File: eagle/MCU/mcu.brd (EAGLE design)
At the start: 100 x 60 mm, 87 parts, among them IC1 HCT4046A, IC10 LD117ADT50TR, IC2 AZ1117-3.3, IC3 4059D, IC4 AZ1086, IC5 74AHCT1G08DCK, IC7 74LVX4245TSSOP24W, IC8 74LVX4245TSSOP24W, IC9 74LVX4245TSSOP24W, T1 2N7002E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

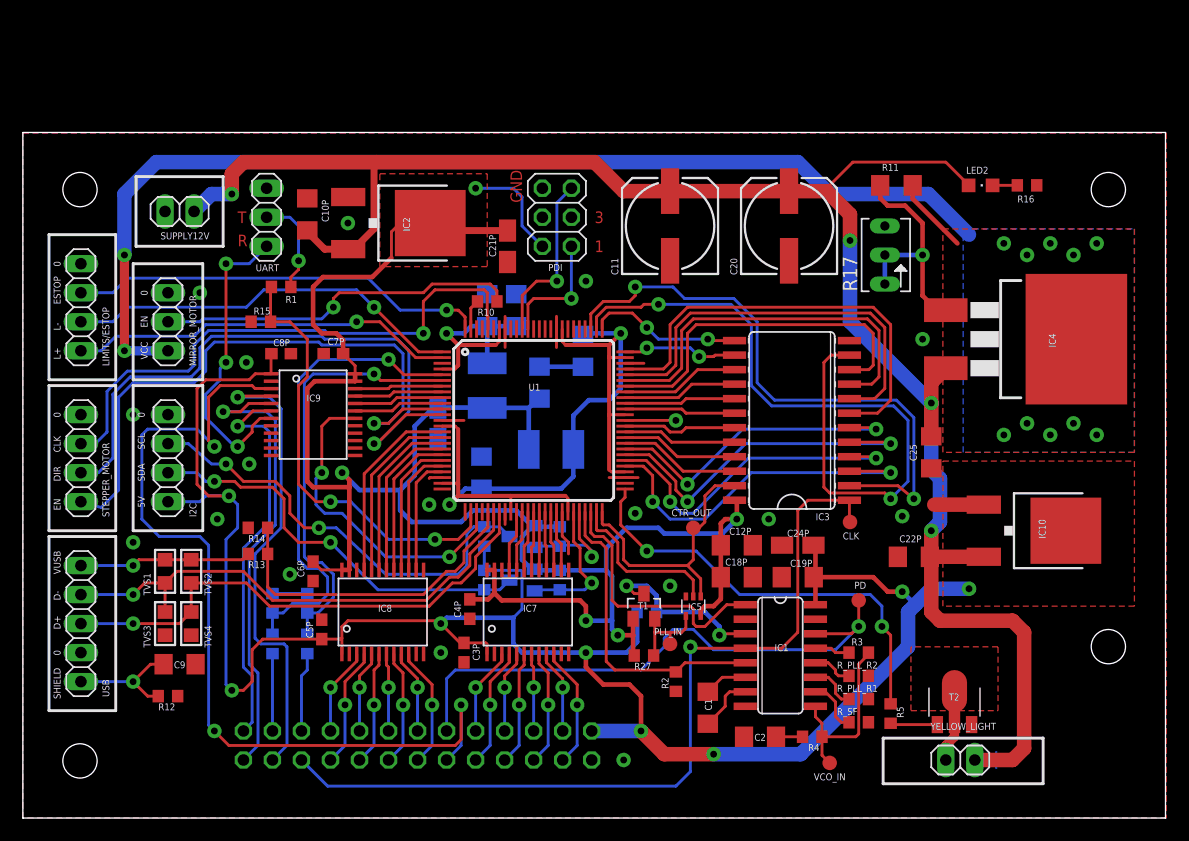
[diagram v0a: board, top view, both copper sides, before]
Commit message: PLL acquires lock
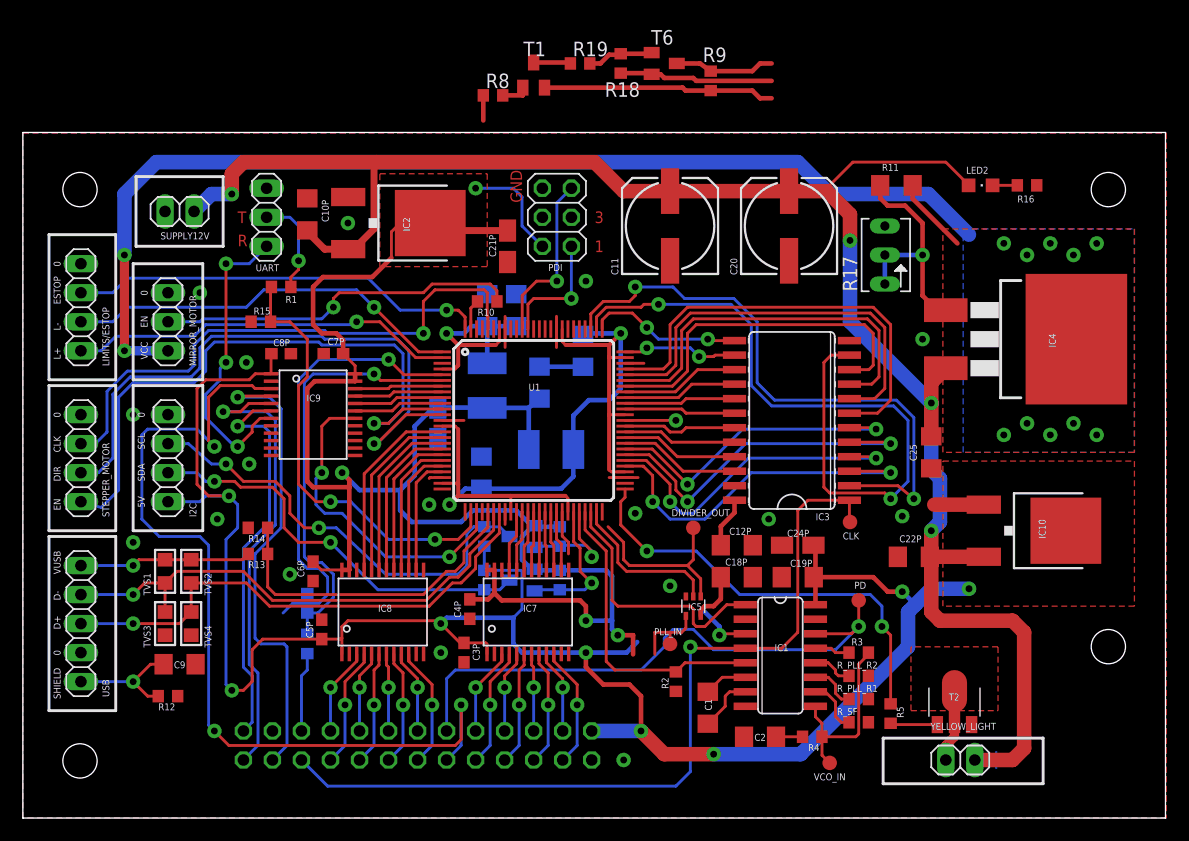
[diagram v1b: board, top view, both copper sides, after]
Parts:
- removed R27, R30: 10kΩ, rcl:R0603
- added R18: 5kΩ, rcl:R0603
- added R19: 10kΩ, rcl:R0603
- added T6: BC857, transistor:SOT23-BEC
- R8: value 500Ω -> 100Ω
- R9: value 1kΩ -> 10kΩ
- T1: value 2N7002E -> BC817; device nxp_60:SOT23 -> transistor:SOT23-BEC
- moved R9 59.7 mm to (60.2, 64.5), flipped to the top, turned to 90 degrees
- moved R8 51.7 mm to (41.1, 63.2), flipped to the top, turned to 0 degrees
- moved T1 47.5 mm to (44.7, 65.0)
- renumbered CTR_OUT to DIVIDER_OUT
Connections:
- removed net DIVIDER_OUT1: IC5.4, PLL_IN.TP, R27.1, T1.2
- new net DIVIDER_OUT_IF_NOT_USING_EVOUT_PD4: U1.50
- new net N$41: R8.2, T1.B
- new net N$42: R19.1, T1.C
- new net PLL_IN_3V3: IC5.4, PLL_IN.TP, R8.1
- new net PLL_IN_5V: IC1.3, R9.2, T6.C
- net DIVIDER_OUT: now also U1.29; no longer IC3.23, U1.50
- net GND: now also T1.E; no longer IC9.17
- net LM_CLK: now also U1.25
- net LM_SYNC: no longer R8.2
- net N$2: now also R18.1, R19.2, T6.B; no longer IC1.3, R30.1, T1.3
- net N$77: no longer R8.1, R9.2
- net VCC/3.3V: no longer C12P.2, IC3.24, R27.2, T1.1
- net VCC/5V: now also C12P.2, IC3.24, R18.2, T6.E; no longer R30.2
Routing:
- net VCC/3.3V: track 178.2 -> 153.8 mm, vias 5 -> 4
- net GND: track 33.4 -> 50.6 mm
- net VCC/5V: track 174.1 -> 189.5 mm
- net PLL_IN_5V: track 0.00 -> 13.7 mm, vias 0 -> 1
- net N$2: track 15.3 -> 5.87 mm, vias 2 -> 0
- net PLL_IN_3V3: track 0.00 -> 9.09 mm
- net DIVIDER_OUT: track 24.2 -> 16.0 mm
- net DIVIDER_OUT1: track 8.22 -> 0.00 mm
- net LM_SYNC: track 6.77 -> 0.00 mm
- net N$42: track 0.00 -> 3.30 mm
- net N$77: track 41.7 -> 38.9 mm
- net N$41: track 0.00 -> 2.43 mm

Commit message: Next version
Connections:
- removed net DIVIDER_OUT_IF_NOT_USING_EVOUT_PD4: U1.50
- new net PD4: U1.29
- net DIVIDER_OUT: now also U1.50; no longer U1.29
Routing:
- net DIVIDER_OUT: track 16.0 -> 17.5 mm
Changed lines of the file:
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@@
 <contactref element="JP1" pad="12"/>
 <wire x1="37.084" y1="12.192" x2="37.084" y2="7.62" width="0.254" layer="16"/>
-<contactref element="IC1" pad="14"/>
 <wire x1="37.084" y1="12.192" x2="37.846" y2="12.954" width="0.254" layer="16"/>
 <wire x1="37.846" y1="12.954" x2="54.102" y2="12.954" width="0.254" layer="16"/>
@@
 <via x="73.152" y="16.764" extent="1-16" drill="0.6" diameter="1.27" shape="octagon"/>
 <wire x1="71.12" y1="14.732" x2="73.152" y2="16.764" width="0.254" layer="16"/>
-<wire x1="69.3674" y1="16.129" x2="72.517" y2="16.129" width="0.254" layer="1"/>
-<wire x1="72.517" y1="16.129" x2="73.152" y2="16.764" width="0.254" layer="1"/>
 <contactref element="PD" pad="TP"/>
 <wire x1="73.152" y1="16.764" x2="73.152" y2="19.05" width="0.254" layer="1"/>
@@
 <wire x1="58.674" y1="16.51" x2="60.452" y2="14.732" width="0.254" layer="16"/>
 <wire x1="60.452" y1="14.732" x2="71.12" y2="14.732" width="0.254" layer="16"/>
+<contactref element="IC1" pad="14"/>
+<wire x1="69.3674" y1="16.129" x2="72.517" y2="16.129" width="0.254" layer="1"/>
+<wire x1="72.517" y1="16.129" x2="73.152" y2="16.764" width="0.254" layer="1"/>
 </signal>
 <signal name="PLL_IN_5V">
@@
 <wire x1="72.3392" y1="35.433" x2="74.803" y2="35.433" width="0.254" layer="1"/>
 </signal>
-<signal name="DIVIDER_OUT">
-<contactref element="IC5" pad="1"/>
-<contactref element="DIVIDER_OUT" pad="TP"/>
-<wire x1="51.212" y1="25.496" x2="52.578" y2="24.13" width="0.254" layer="1"/>
-<wire x1="52.578" y1="24.13" x2="52.578" y2="22.606" width="0.254" layer="1"/>
-<wire x1="52.578" y1="22.606" x2="53.086" y2="22.098" width="0.254" layer="1"/>
-<wire x1="53.086" y1="22.098" x2="58.166" y2="22.098" width="0.254" layer="1"/>
-<wire x1="58.674" y1="25.4" x2="58.674" y2="22.606" width="0.254" layer="1"/>
-<wire x1="59.324" y1="19.392" x2="59.324" y2="20.94" width="0.254" layer="1"/>
-<wire x1="59.324" y1="20.94" x2="58.166" y2="22.098" width="0.254" layer="1"/>
-<wire x1="58.674" y1="22.606" x2="58.166" y2="22.098" width="0.254" layer="1"/>
+<signal name="PD4">
 <contactref element="U1" pad="29"/>
-<wire x1="40.204" y1="26.798" x2="51.212" y2="25.496" width="0" layer="19" extent="1-1"/>
 </signal>
 <signal name="LM_DATA_5V0">
@@
 <wire x1="87.034" y1="55.372" x2="84.87" y2="55.372" width="0.254" layer="1"/>
 </signal>
-<signal name="DIVIDER_OUT_IF_NOT_USING_EVOUT_PD4">
+<signal name="DIVIDER_OUT">
 <contactref element="U1" pad="50"/>
+<contactref element="IC5" pad="1"/>
+<contactref element="DIVIDER_OUT" pad="TP"/>
+<wire x1="50.704" y1="26.004" x2="52.578" y2="24.13" width="0.254" layer="1"/>
+<wire x1="52.578" y1="24.13" x2="52.578" y2="22.606" width="0.254" layer="1"/>
+<wire x1="52.578" y1="22.606" x2="53.086" y2="22.098" width="0.254" layer="1"/>
+<wire x1="53.086" y1="22.098" x2="58.166" y2="22.098" width="0.254" layer="1"/>
+<wire x1="58.674" y1="25.4" x2="58.674" y2="22.606" width="0.254" layer="1"/>
+<wire x1="59.324" y1="19.392" x2="59.324" y2="20.94" width="0.254" layer="1"/>
+<wire x1="59.324" y1="20.94" x2="58.166" y2="22.098" width="0.254" layer="1"/>
+<wire x1="58.674" y1="22.606" x2="58.166" y2="22.098" width="0.254" layer="1"/>
+<wire x1="50.704" y1="26.004" x2="50.704" y2="26.798" width="0.254" layer="1"/>
 </signal>
 <signal name="N$41">
